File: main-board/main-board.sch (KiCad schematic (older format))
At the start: 73 parts, among them J1 MOTOR0, J10 PROGRAMMER, J11 CAM0, J12 CAM1, J13 CAM2, J14 CAM3, J15 CAM4, J16 CAM5, J17 CAM6, J18 CAM7, J19 PowerBoard Interface, J2 MOTOR1, J20 IMU Breakout, J21 ICSP (DO NOT POPULATE), J3 MOTOR2, J4 MOTOR3, J5 RJ45, J6 MOTOR4, J7 MOTOR5, J8 MOTOR6, J9 MOTOR7, SW1 SW_SPST, T1 ATB2012E-50011M-T01, T2 ATB2012E-50011M-T01, U1 MCP2515-EST, U2 ATA6560, U3 ATmega2560-16AU | Main Proc, U4 MC14051B, U5 MC14051B, U6 SN75HVD3082EDR, U7 LTC1983ES6-5-TRPBF, U8 THS7314DR, U9 SN75HVD3082EDR, Y1 20MHz, Y2 20MHz

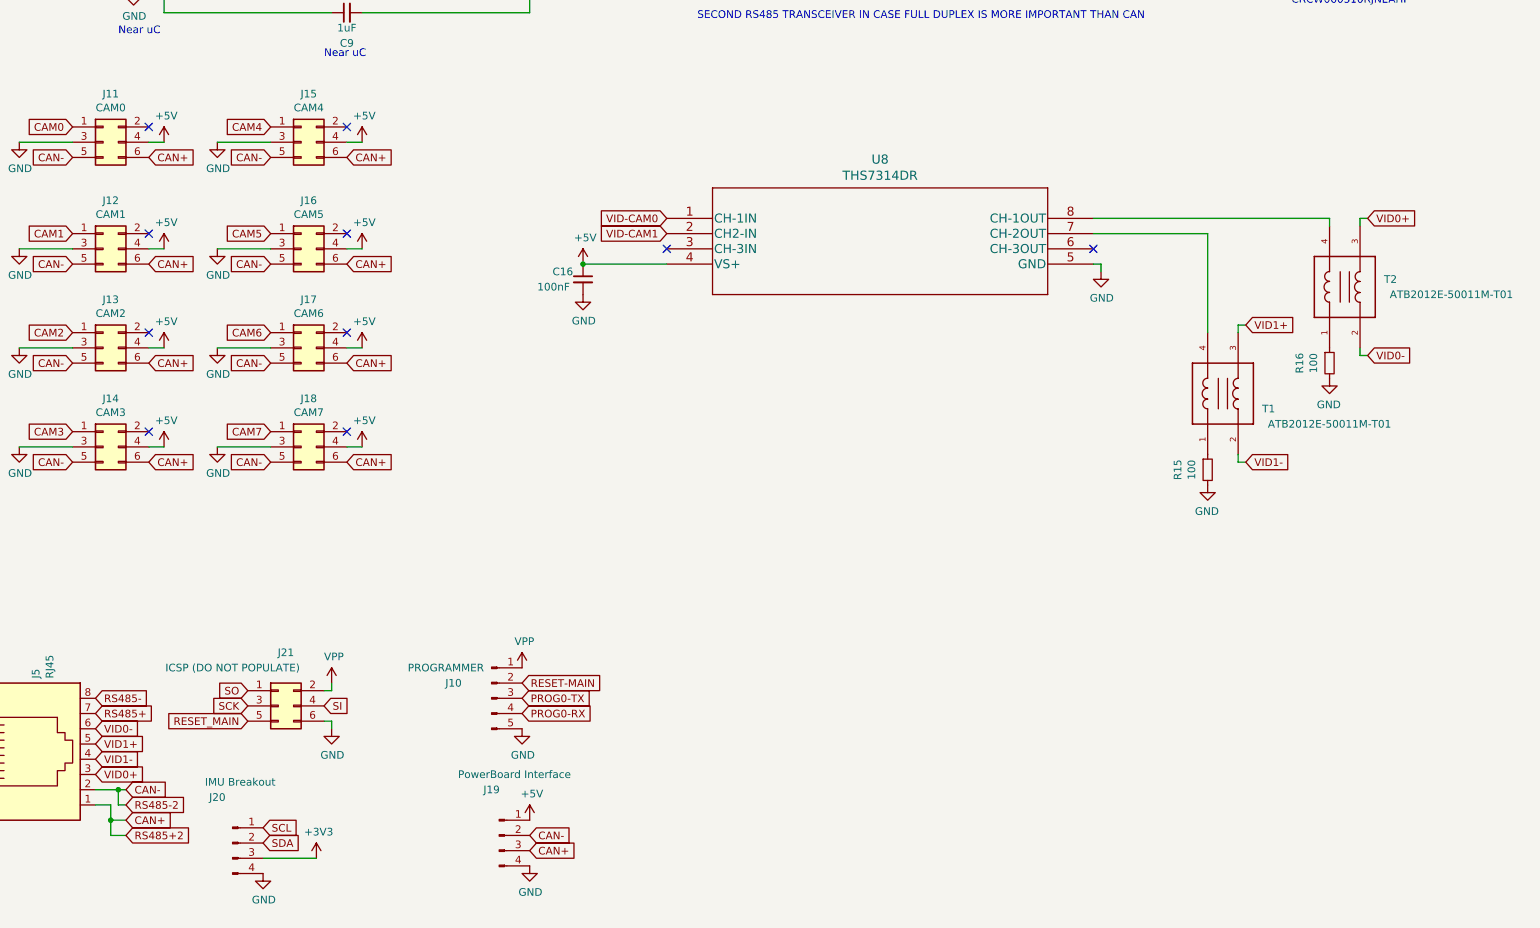
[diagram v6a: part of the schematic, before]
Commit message: S 1.0.1 B 1.0.1 change camera balancing to MAX4449ESE
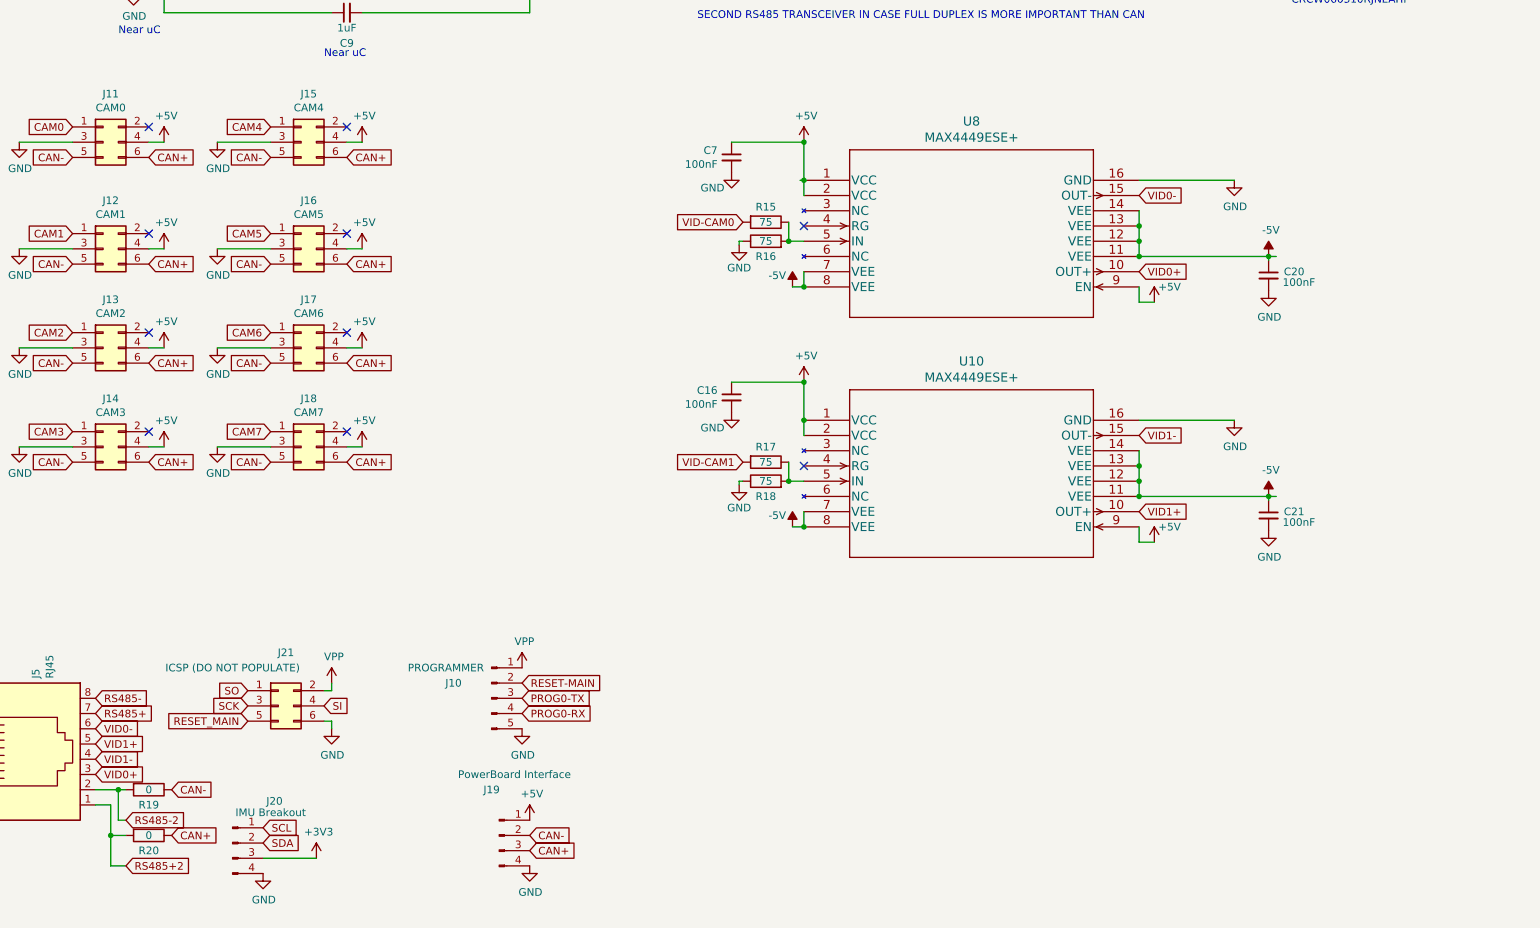
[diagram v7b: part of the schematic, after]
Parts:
- removed R15, R16: 100, Resistor_SMD:R_0603_1608Metric, symbol Device:R_Small
- removed T1, T2: ATB2012E-50011M-T01, HHM1595A1:BALUN_HHM1595A1, symbol main-board-rescue:ATB2012E-50011M-T01-ATB2012E-50011M-T01
- removed U8: THS7314DR, ths7314dr:THS7314DR, symbol ths7314dr:THS7314DR
- added C20, C21, C7: 100nF, Capacitor_SMD:C_0603_1608Metric, symbol Device:C_Small
- added R15, R16, R17, R18: 75, Resistor_SMD:R_0603_1608Metric, symbol Device:R
- added R19, R20: 0, Resistor_SMD:R_0603_1608Metric, symbol Device:R
- added U10, U8: MAX4449ESE+, MAX4449ESE:MAX4449ESE&plus_, symbol MAX4449ESE:MAX4449ESE+
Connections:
- net +5V: now also C7.1, U10.1 (VCC), U10.2 (VCC), U10.9 (EN), U8.1 (VCC), U8.2 (VCC), U8.9 (EN)
- net -5V: now also C20.1, C21.1, U10.11 (VEE), U10.12 (VEE), U10.13 (VEE), U10.14 (VEE), U10.7 (VEE), U10.8 (VEE), U8.11 (VEE), U8.12 (VEE), U8.13 (VEE), U8.14 (VEE), U8.7 (VEE), U8.8 (VEE)
- net CAN+: now also R20.1; no longer D4.1 (IO1), J5.1, R13.1
- net CAN-: now also R19.1; no longer D4.2 (IO2), J5.2, R14.1
- net GND: now also C20.2, C21.2, C7.2, R16.1, R18.1, U10.16 (GND), U8.16 (GND)
- net VID-CAM0: now also R15.2
- net VID-CAM1: now also R17.2
- net VID0+: now also U8.10 (OUT+)
- net VID0-: now also U8.15 (OUT-)
- net VID1+: now also U10.10 (OUT+)
- net VID1-: now also U10.15 (OUT-)
- new net: R17.1, R18.2, U10.5 (IN)
- new net: R15.1, R16.2, U8.5 (IN)
- new net RS485+2: D4.1 (IO1), J5.1, R13.1, R20.2
- new net RS485-2: D4.2 (IO2), J5.2, R14.1, R19.2

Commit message: Removing old routes to support full duplex rs485
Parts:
- removed C19: 100nF, Capacitor_SMD:C_0603_1608Metric, symbol Device:C_Small
- removed D2, D4: CDSOT23-SM712, Package_TO_SOT_SMD:SOT-23, symbol main-board-rescue:CDSOT23-SM712-CDSOT23-SM712
- removed J5: RJ45, Connector_PinHeader_2.54mm:PinHeader_1x08_P2.54mm_Vertical, symbol Connector:RJ45
- removed R10, R11, R13, R14: 10, Resistor_SMD:R_0603_1608Metric, symbol Device:R_Small
- removed R12, R5, R8, R9: 10k, Resistor_SMD:R_0603_1608Metric, symbol Device:R_Small
- removed U6, U9: SN75HVD3082EDR, Package_SO:SOIC-8_3.9x4.9mm_P1.27mm, symbol main-board-rescue:SN75HVD3082EDR-SN75HVD3082EDR_
- added J5: Tether Interface, Connector_PinHeader_2.54mm:PinHeader_2x06_P2.54mm_Vertical, symbol Connector_Generic:Conn_02x06_Counter_Clockwise
- added R5, R8: 120, Resistor_SMD:R_0603_1608Metric, symbol Device:R
- added U6: MAX490E, Package_SO:SOIC-8_3.9x4.9mm_P1.27mm, symbol Interface_UART:MAX490E
- U10, U8: symbol MAX4449ESE:MAX4449ESE+ -> main-board-rescue:MAX4449ESE+-MAX4449ESE
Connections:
- net +5V: now also U6.1 (VCC)
- net CAN+: now also R5.2
- net CAN-: now also R5.1
- net GND: now also U6.4 (GND)
- net VID0+: now also J5.4 (Pin_4)
- net VID0-: now also J5.3 (Pin_3)
- net VID1+: now also J5.2 (Pin_2)
- net VID1-: now also J5.1 (Pin_1)
- net RS485+2: no longer names the net of R20.2
- net RS485+2: now also J5.7 (Pin_7)
- net RS485-2: no longer names the net of R19.2
- net RS485-2: now also J5.8 (Pin_8)
- net RS485-D renamed D
- net D: now also U6.3 (DI)
- net RS485-DIR: no longer names the net of U3.14 (PH2)
- net RS485-R renamed R
- net R: now also U6.2 (RO)
- new net RX_H: J5.10 (Pin_10), U6.5 (Y)
- new net RX_L: J5.9 (Pin_9), U6.6 (Z)
- new net TX_H: J5.12 (Pin_12), R8.2, U6.8 (A)
- new net TX_L: J5.11 (Pin_11), R8.1, U6.7 (B)
- no-connect marks 68 -> 69
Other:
- note removed: "Pulse-Proof Thick-Film Resistor\nCRCW060310RJNEAHP\n"
- note removed: "SECOND RS485 TRANSCEIVER IN CASE FULL DUPLEX IS MORE IMPORTANT THAN CAN"
- moved on the sheet: J20, J21, R19, R20, R6, R7
